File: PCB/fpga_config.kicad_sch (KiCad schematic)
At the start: 11 parts, among them J10 Pin header, 1x4, U4 LFE5U-25F-6BG256C, U5 W25Q128JVSIQ

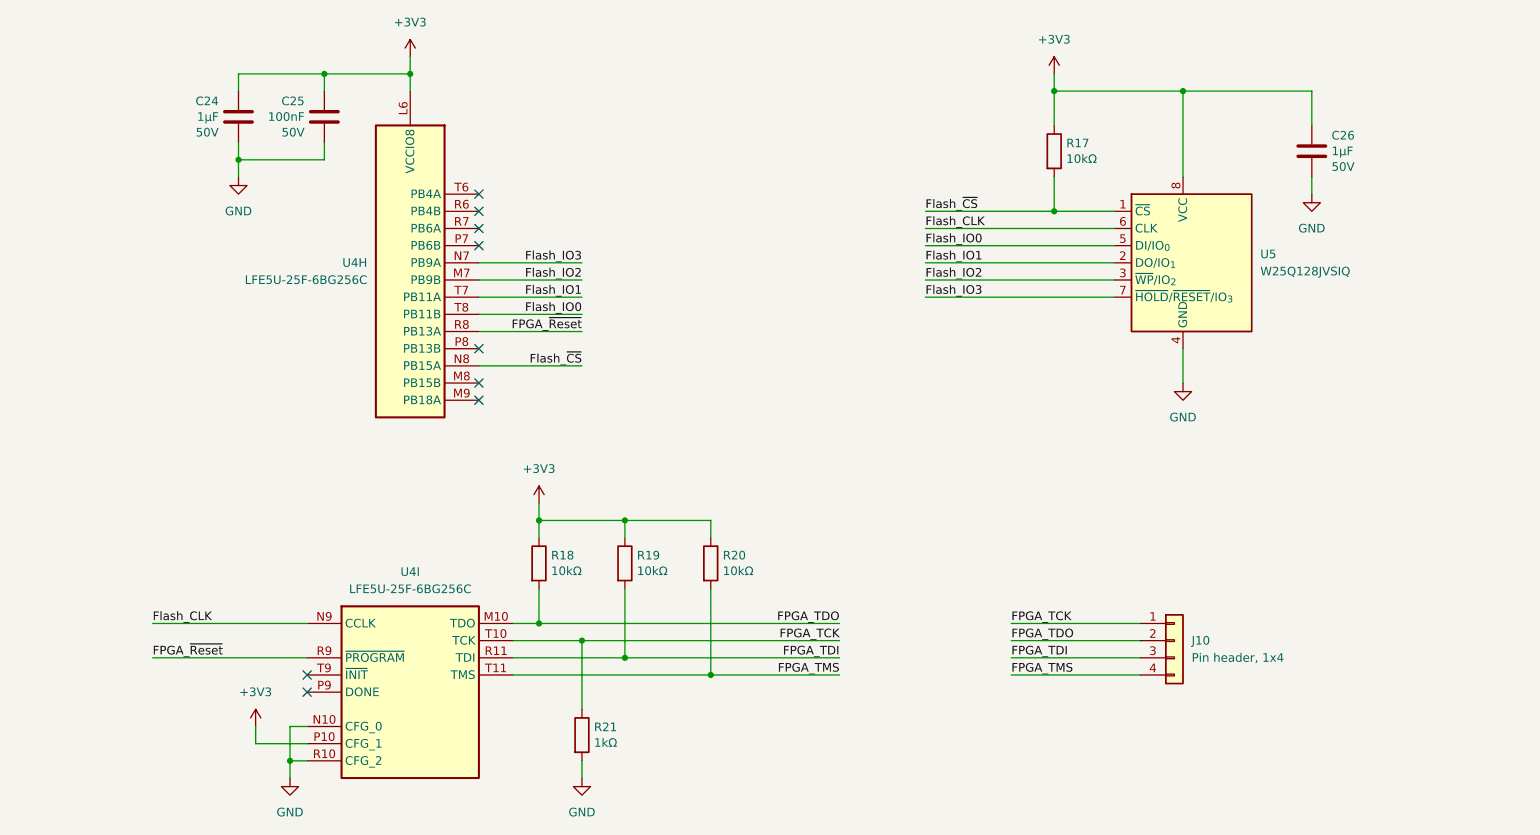
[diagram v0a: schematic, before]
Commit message: Add ESD protection
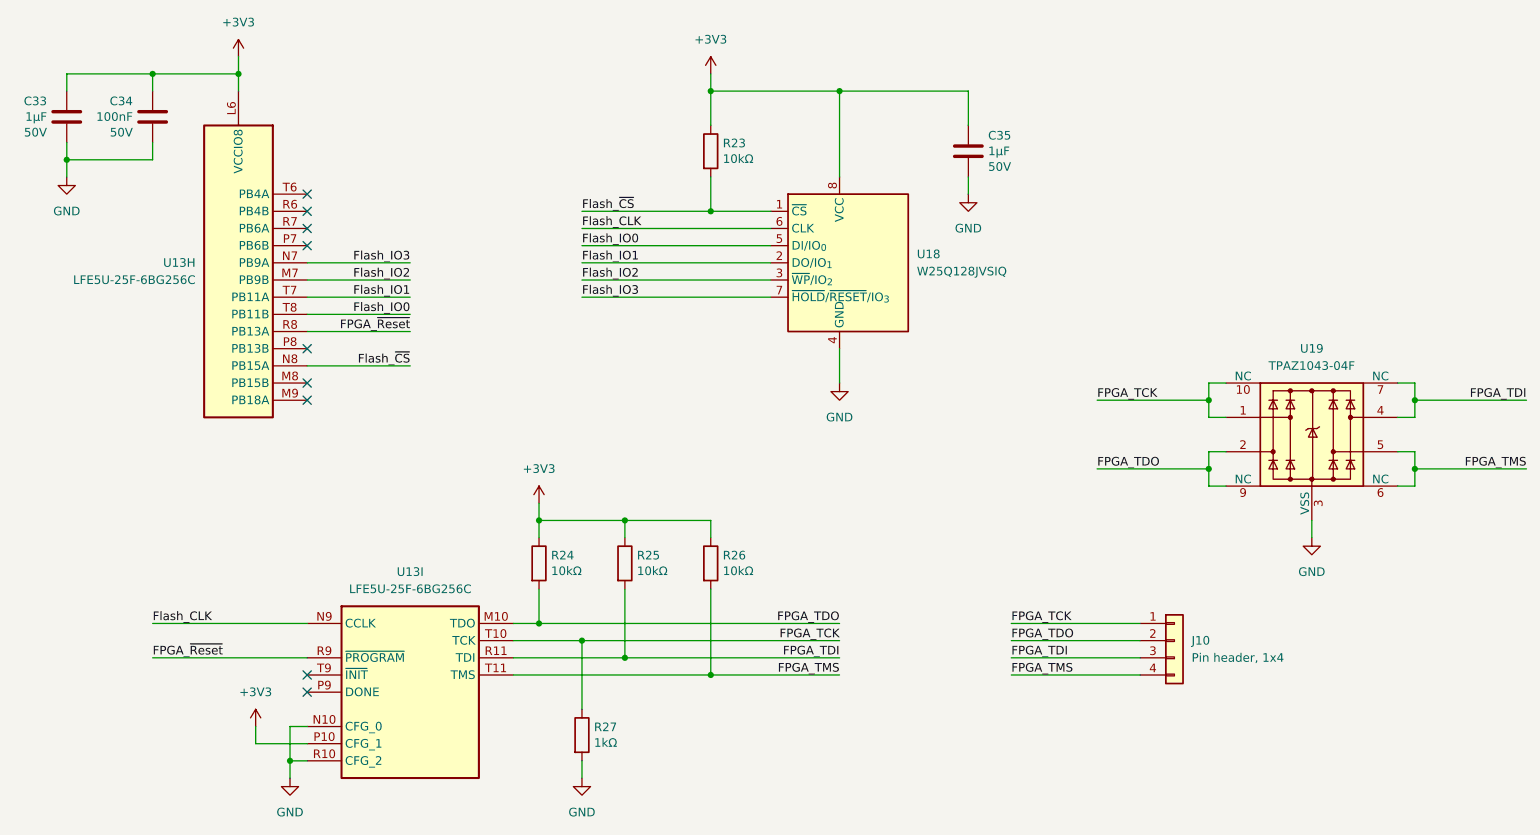
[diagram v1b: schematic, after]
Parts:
- added U19: TPAZ1043-04F, Package_DFN_QFN:Diodes_UDFN-10_1.0x2.5mm_P0.5mm, symbol Power_Protection:D3V3XA4B10LP
- renumbered C24 to C33, C25 to C34, C26 to C35, R17 to R23, R18 to R24, R19 to R25, R20 to R26, R21 to R27, U4 to U13, U5 to U18
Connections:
- net FPGA_TCK: now also U19.1, U19.10 (NC)
- net FPGA_TDI: now also U19.4, U19.7 (NC)
- net FPGA_TDO: now also U19.2, U19.9 (NC)
- net FPGA_TMS: now also U19.5, U19.6 (NC)
- net GND: now also U19.3 (VSS), U19.8 (VSS)
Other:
- moved on the sheet: C33, C34, C35, R23, U13H, U18

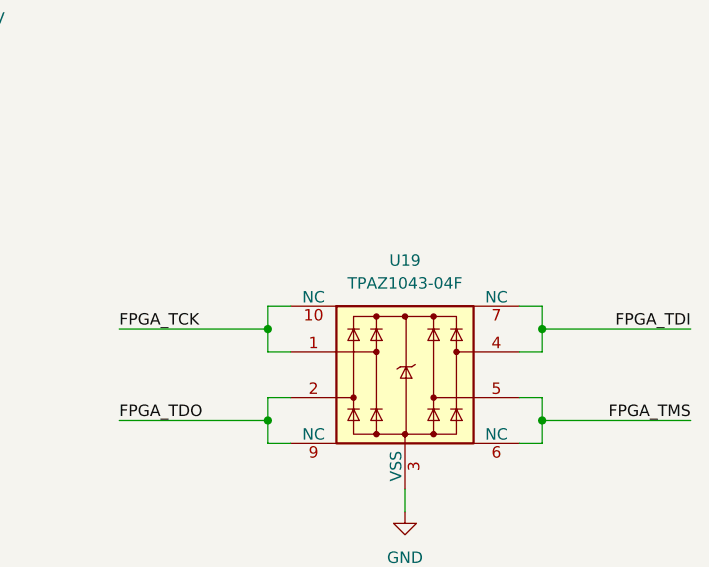
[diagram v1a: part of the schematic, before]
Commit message: Improve the ESD protection
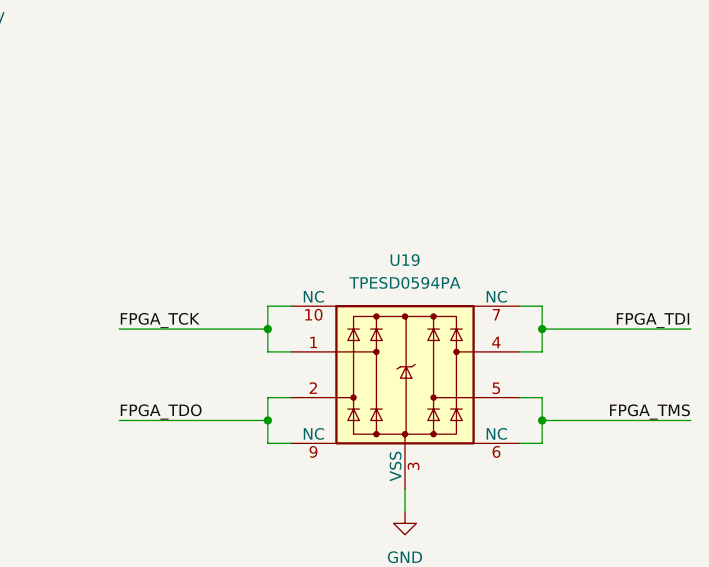
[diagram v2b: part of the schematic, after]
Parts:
- U19: value TPAZ1043-04F -> TPESD0594PA; LCSC C2827673 -> C42436622; Part_number TPAZ1043-04F -> TPESD0594PA
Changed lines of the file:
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@@
 		(dnp no)
 		(fields_autoplaced yes)
-		(property "Reference" "#PWR067"
+		(property "Reference" "#PWR069"
 			(at 165.1 100.33 0)
 			(effects
@@
 			(project "clavier"
 				(path "/6362c6e0-59ef-40d3-b6e0-7e9dfe7b9b20/d73938da-f0ba-48e3-aac9-a36988c25c2c/de1eff49-f476-44bd-be62-918dcb8e6e8d"
-					(reference "#PWR067")
+					(reference "#PWR069")
 					(unit 1)
 				)
@@
 		(dnp no)
 		(fields_autoplaced yes)
-		(property "Reference" "#PWR063"
+		(property "Reference" "#PWR065"
 			(at 76.2 49.53 0)
 			(effects
@@
 			(project ""
 				(path "/6362c6e0-59ef-40d3-b6e0-7e9dfe7b9b20/d73938da-f0ba-48e3-aac9-a36988c25c2c/de1eff49-f476-44bd-be62-918dcb8e6e8d"
-					(reference "#PWR063")
+					(reference "#PWR065")
 					(unit 1)
 				)
@@
 		(dnp no)
 		(fields_autoplaced yes)
-		(property "Reference" "#PWR068"
+		(property "Reference" "#PWR070"
 			(at 120.65 115.57 0)
 			(effects
@@
 			(project "clavier"
 				(path "/6362c6e0-59ef-40d3-b6e0-7e9dfe7b9b20/d73938da-f0ba-48e3-aac9-a36988c25c2c/de1eff49-f476-44bd-be62-918dcb8e6e8d"
-					(reference "#PWR068")
+					(reference "#PWR070")
 					(unit 1)
 				)
@@
 		(dnp no)
 		(fields_autoplaced yes)
-		(property "Reference" "#PWR066"
+		(property "Reference" "#PWR068"
 			(at 184.15 72.39 0)
 			(effects
@@
 			(project "clavier"
 				(path "/6362c6e0-59ef-40d3-b6e0-7e9dfe7b9b20/d73938da-f0ba-48e3-aac9-a36988c25c2c/de1eff49-f476-44bd-be62-918dcb8e6e8d"
-					(reference "#PWR066")
+					(reference "#PWR068")
 					(unit 1)
 				)
@@
 			)
 		)
-		(property "Value" "TPAZ1043-04F"
+		(property "Value" "TPESD0594PA"
 			(at 234.95 91.44 0)
 			(effects
@@
 			)
 		)
-		(property "Datasheet" "https://www.lcsc.com/datasheet/lcsc_datasheet_2411121100_TECH-PUBLIC-TPAZ1043-04F_C2827673.pdf"
+		(property "Datasheet" "https://www.lcsc.com/datasheet/lcsc_datasheet_2501161435_TECH-PUBLIC-TPESD0594PA_C42436622.pdf"
 			(at 234.95 101.6 0)
 			(effects
@@
 			)
 		)
-		(property "LCSC" "C2827673"
+		(property "LCSC" "C42436622"
 			(at 234.95 101.6 0)
 			(effects
@@
 			)
 		)
-		(property "Part_number" "TPAZ1043-04F"
+		(property "Part_number" "TPESD0594PA"
 			(at 234.95 101.6 0)
 			(effects
@@
 		(dnp no)
 		(fields_autoplaced yes)
-		(property "Reference" "#PWR064"
+		(property "Reference" "#PWR066"
 			(at 146.05 52.07 0)
 			(effects
@@
 			(project "clavier"
 				(path "/6362c6e0-59ef-40d3-b6e0-7e9dfe7b9b20/d73938da-f0ba-48e3-aac9-a36988c25c2c/de1eff49-f476-44bd-be62-918dcb8e6e8d"
-					(reference "#PWR064")
+					(reference "#PWR066")
 					(unit 1)
 				)
@@
 		(dnp no)
 		(fields_autoplaced yes)
-		(property "Reference" "#PWR071"
+		(property "Reference" "#PWR073"
 			(at 83.82 158.75 0)
 			(effects
@@
 			(project "clavier"
 				(path "/6362c6e0-59ef-40d3-b6e0-7e9dfe7b9b20/d73938da-f0ba-48e3-aac9-a36988c25c2c/de1eff49-f476-44bd-be62-918dcb8e6e8d"
-					(reference "#PWR071")
+					(reference "#PWR073")
 					(unit 1)
 				)
@@
 		(dnp no)
 		(fields_autoplaced yes)
-		(property "Reference" "#PWR072"
+		(property "Reference" "#PWR074"
 			(at 127 158.75 0)
 			(effects
@@
 			(project "clavier"
 				(path "/6362c6e0-59ef-40d3-b6e0-7e9dfe7b9b20/d73938da-f0ba-48e3-aac9-a36988c25c2c/de1eff49-f476-44bd-be62-918dcb8e6e8d"
-					(reference "#PWR072")
+					(reference "#PWR074")
 					(unit 1)
 				)
@@
 		(dnp no)
 		(fields_autoplaced yes)
-		(property "Reference" "#PWR070"
+		(property "Reference" "#PWR072"
 			(at 78.74 148.59 0)
 			(effects
@@
 			(project "clavier"
 				(path "/6362c6e0-59ef-40d3-b6e0-7e9dfe7b9b20/d73938da-f0ba-48e3-aac9-a36988c25c2c/de1eff49-f476-44bd-be62-918dcb8e6e8d"
-					(reference "#PWR070")
+					(reference "#PWR072")
 					(unit 1)
 				)
@@
 		(dnp no)
 		(fields_autoplaced yes)
-		(property "Reference" "#PWR069"
+		(property "Reference" "#PWR071"
 			(at 234.95 123.19 0)
 			(effects
@@
 			(project "clavier"
 				(path "/6362c6e0-59ef-40d3-b6e0-7e9dfe7b9b20/d73938da-f0ba-48e3-aac9-a36988c25c2c/de1eff49-f476-44bd-be62-918dcb8e6e8d"
-					(reference "#PWR069")
+					(reference "#PWR071")
 					(unit 1)
 				)
@@
 		(dnp no)
 		(fields_autoplaced yes)
-		(property "Reference" "#PWR065"
+		(property "Reference" "#PWR067"
 			(at 50.8 69.85 0)
 			(effects
@@
 			(project "clavier"
 				(path "/6362c6e0-59ef-40d3-b6e0-7e9dfe7b9b20/d73938da-f0ba-48e3-aac9-a36988c25c2c/de1eff49-f476-44bd-be62-918dcb8e6e8d"
-					(reference "#PWR065")
+					(reference "#PWR067")
 					(unit 1)
 				)

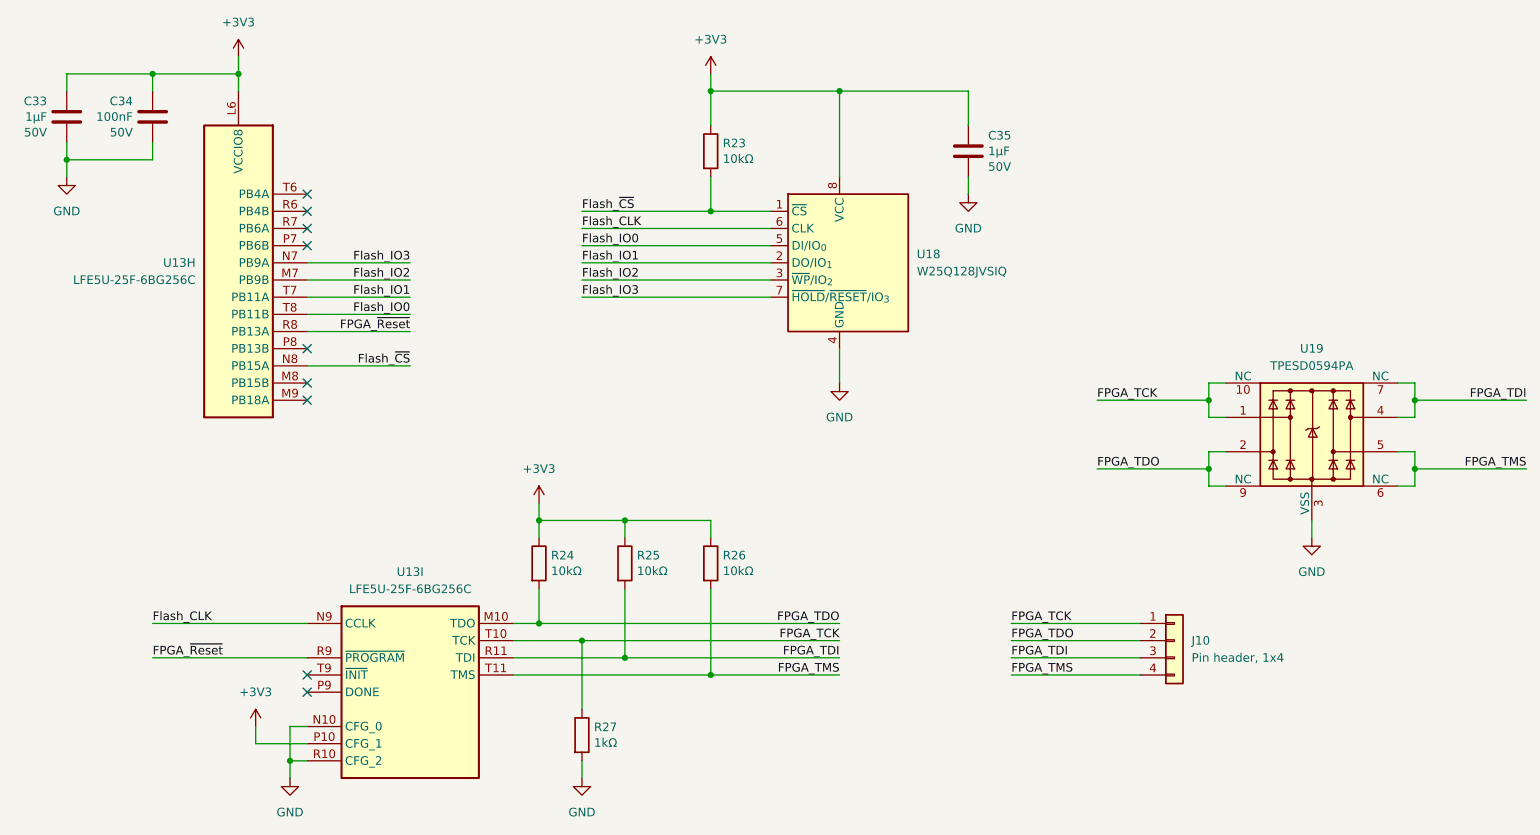
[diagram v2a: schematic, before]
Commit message: Complete the PCB routing
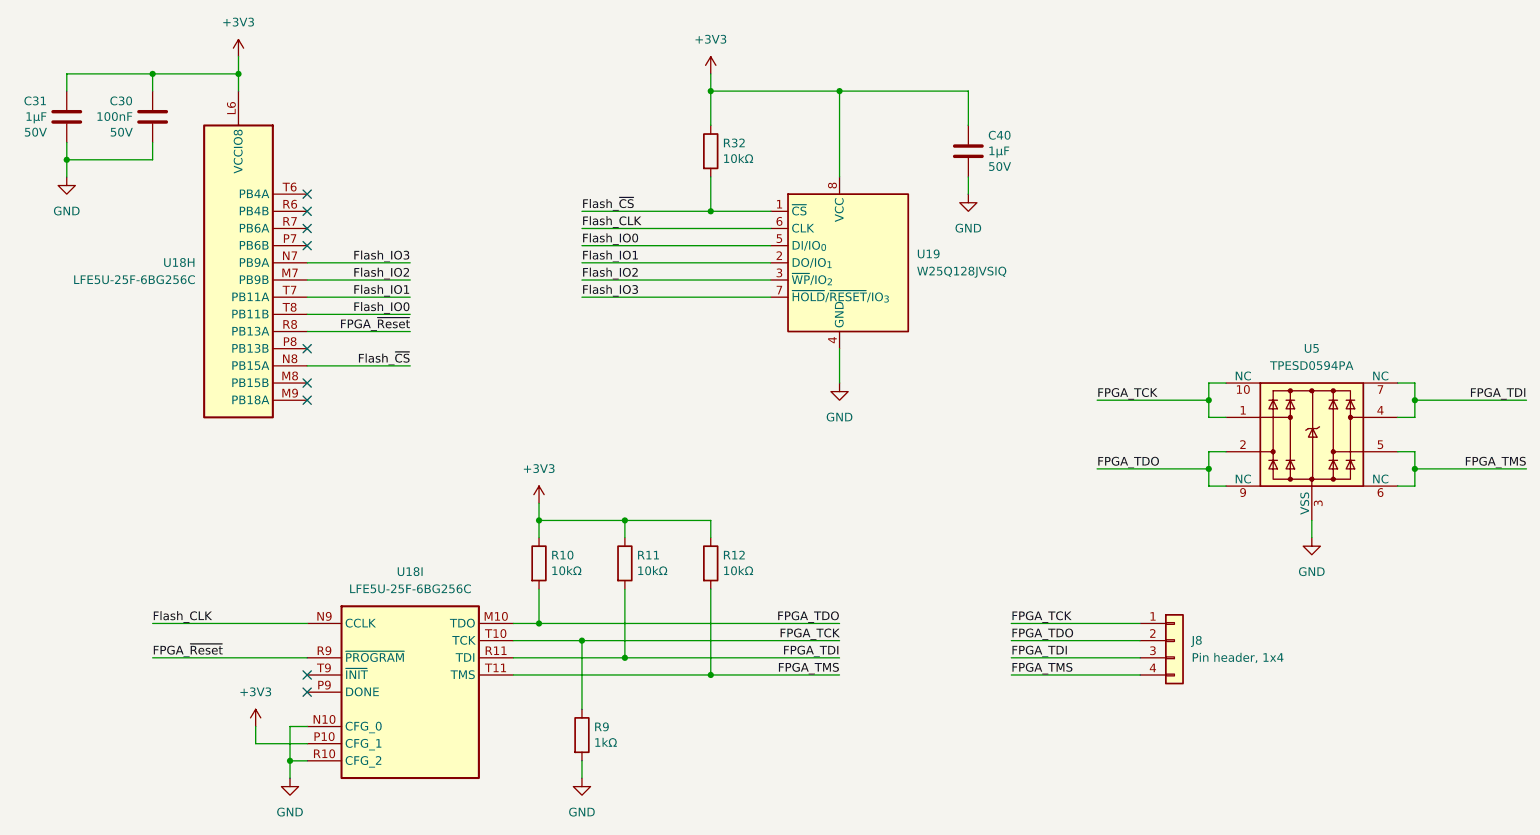
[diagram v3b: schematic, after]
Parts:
- renumbered C34 to C30, C33 to C31, C35 to C40, J10 to J8, R24 to R10, R25 to R11, R26 to R12, R23 to R32, R27 to R9, U13 to U18, U18 to U19, U19 to U5
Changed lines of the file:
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@@
 	(title_block
 		(title "Clavier - FPGA configuration")
-		(date "2025-06-21")
+		(date "2025-06-22")
 		(rev "1.0")
 		(company "Copyright (c) 2025 L. Sartory")
@@
 		(on_board yes)
 		(dnp no)
-		(property "Reference" "R27"
+		(property "Reference" "R9"
 			(at 128.778 144.8816 0)
 			(effects
@@
 			(project "clavier"
 				(path "/6362c6e0-59ef-40d3-b6e0-7e9dfe7b9b20/d73938da-f0ba-48e3-aac9-a36988c25c2c/de1eff49-f476-44bd-be62-918dcb8e6e8d"
-					(reference "R27")
+					(reference "R9")
 					(unit 1)
 				)
@@
 		(on_board yes)
 		(dnp no)
-		(property "Reference" "R23"
+		(property "Reference" "R32"
 			(at 147.828 58.5216 0)
 			(effects
@@
 			(project "clavier"
 				(path "/6362c6e0-59ef-40d3-b6e0-7e9dfe7b9b20/d73938da-f0ba-48e3-aac9-a36988c25c2c/de1eff49-f476-44bd-be62-918dcb8e6e8d"
-					(reference "R23")
+					(reference "R32")
 					(unit 1)
 				)
@@
 		(on_board yes)
 		(dnp no)
-		(property "Reference" "C35"
+		(property "Reference" "C40"
 			(at 187.071 57.3786 0)
 			(effects
@@
 			(project "clavier"
 				(path "/6362c6e0-59ef-40d3-b6e0-7e9dfe7b9b20/d73938da-f0ba-48e3-aac9-a36988c25c2c/de1eff49-f476-44bd-be62-918dcb8e6e8d"
-					(reference "C35")
+					(reference "C40")
 					(unit 1)
 				)
@@
 		(dnp no)
 		(fields_autoplaced yes)
-		(property "Reference" "J10"
+		(property "Reference" "J8"
 			(at 217.17 132.0799 0)
 			(effects
@@
 		)
 		(instances
-			(project ""
+			(project "clavier"
 				(path "/6362c6e0-59ef-40d3-b6e0-7e9dfe7b9b20/d73938da-f0ba-48e3-aac9-a36988c25c2c/de1eff49-f476-44bd-be62-918dcb8e6e8d"
-					(reference "J10")
+					(reference "J8")
 					(unit 1)
 				)
@@
 		(on_board yes)
 		(dnp no)
-		(property "Reference" "C34"
+		(property "Reference" "C30"
 			(at 60.579 52.2986 0)
 			(effects
@@
 			(project "clavier"
 				(path "/6362c6e0-59ef-40d3-b6e0-7e9dfe7b9b20/d73938da-f0ba-48e3-aac9-a36988c25c2c/de1eff49-f476-44bd-be62-918dcb8e6e8d"
-					(reference "C34")
+					(reference "C30")
 					(unit 1)
 				)
@@
 		(on_board yes)
 		(dnp no)
-		(property "Reference" "C33"
+		(property "Reference" "C31"
 			(at 47.879 52.2986 0)
 			(effects
@@
 			(project "clavier"
 				(path "/6362c6e0-59ef-40d3-b6e0-7e9dfe7b9b20/d73938da-f0ba-48e3-aac9-a36988c25c2c/de1eff49-f476-44bd-be62-918dcb8e6e8d"
-					(reference "C33")
+					(reference "C31")
 					(unit 1)
 				)
@@
 		(dnp no)
 		(fields_autoplaced yes)
-		(property "Reference" "U19"
+		(property "Reference" "U5"
 			(at 234.95 88.9 0)
 			(effects
@@
 			(project "clavier"
 				(path "/6362c6e0-59ef-40d3-b6e0-7e9dfe7b9b20/d73938da-f0ba-48e3-aac9-a36988c25c2c/de1eff49-f476-44bd-be62-918dcb8e6e8d"
-					(reference "U19")
+					(reference "U5")
 					(unit 1)
 				)
@@
 		(dnp no)
 		(fields_autoplaced yes)
-		(property "Reference" "U13"
+		(property "Reference" "U18"
 			(at 101.6 121.92 0)
 			(effects
@@
 			(project "clavier"
 				(path "/6362c6e0-59ef-40d3-b6e0-7e9dfe7b9b20/d73938da-f0ba-48e3-aac9-a36988c25c2c/de1eff49-f476-44bd-be62-918dcb8e6e8d"
-					(reference "U13")
+					(reference "U18")
 					(unit 9)
 				)
@@
 		(dnp no)
 		(fields_autoplaced yes)
-		(property "Reference" "U13"
+		(property "Reference" "U18"
 			(at 69.85 76.1999 0)
 			(effects
@@
 			(project "clavier"
 				(path "/6362c6e0-59ef-40d3-b6e0-7e9dfe7b9b20/d73938da-f0ba-48e3-aac9-a36988c25c2c/de1eff49-f476-44bd-be62-918dcb8e6e8d"
-					(reference "U13")
+					(reference "U18")
 					(unit 8)
 				)
@@
 		(on_board yes)
 		(dnp no)
-		(property "Reference" "R26"
+		(property "Reference" "R12"
 			(at 147.828 119.4816 0)
 			(effects
@@
 			(project "clavier"
 				(path "/6362c6e0-59ef-40d3-b6e0-7e9dfe7b9b20/d73938da-f0ba-48e3-aac9-a36988c25c2c/de1eff49-f476-44bd-be62-918dcb8e6e8d"
-					(reference "R26")
+					(reference "R12")
 					(unit 1)
 				)
@@
 		(dnp no)
 		(fields_autoplaced yes)
-		(property "Reference" "U18"
+		(property "Reference" "U19"
 			(at 176.53 74.9299 0)
 			(effects
@@
 			(project ""
 				(path "/6362c6e0-59ef-40d3-b6e0-7e9dfe7b9b20/d73938da-f0ba-48e3-aac9-a36988c25c2c/de1eff49-f476-44bd-be62-918dcb8e6e8d"
-					(reference "U18")
+					(reference "U19")
 					(unit 1)
 				)
@@
 		(on_board yes)
 		(dnp no)
-		(property "Reference" "R25"
+		(property "Reference" "R11"
 			(at 135.128 119.4816 0)
 			(effects
@@
 			(project "clavier"
 				(path "/6362c6e0-59ef-40d3-b6e0-7e9dfe7b9b20/d73938da-f0ba-48e3-aac9-a36988c25c2c/de1eff49-f476-44bd-be62-918dcb8e6e8d"
-					(reference "R25")
+					(reference "R11")
 					(unit 1)
 				)
@@
 		(on_board yes)
 		(dnp no)
-		(property "Reference" "R24"
+		(property "Reference" "R10"
 			(at 122.428 119.4816 0)
 			(effects
@@
 			(project "clavier"
 				(path "/6362c6e0-59ef-40d3-b6e0-7e9dfe7b9b20/d73938da-f0ba-48e3-aac9-a36988c25c2c/de1eff49-f476-44bd-be62-918dcb8e6e8d"
-					(reference "R24")
+					(reference "R10")
 					(unit 1)
 				)
